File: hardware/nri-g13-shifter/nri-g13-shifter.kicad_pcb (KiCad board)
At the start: 2 copper layers, 96 x 92 mm, 39 parts, among them J1 NRI G-13 (10 pin), J2 RP2350-Plus, J3 +12V IN, Q1 BSS138, Q2 BSS138, Q3 BSS138, Q4 BSS138, Q5 BSS138, Q6 BSS138, Q7 BSS138

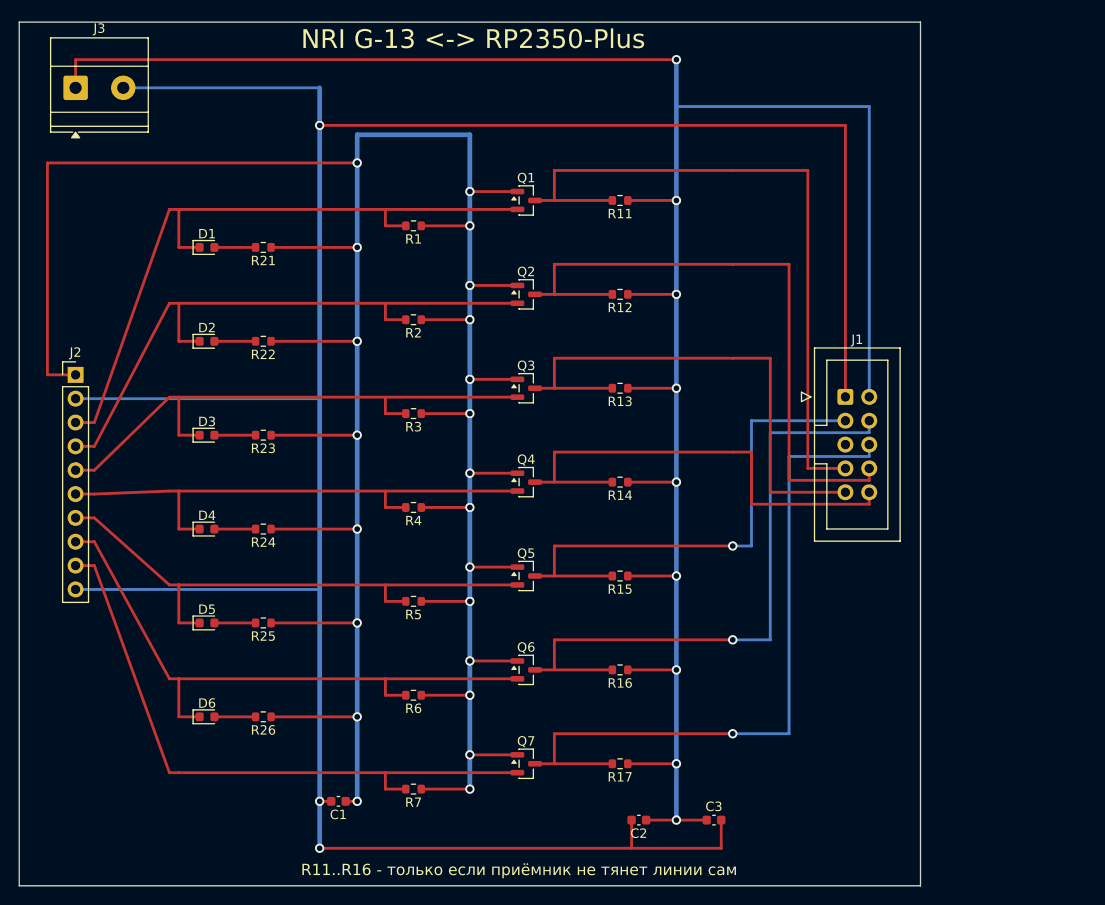
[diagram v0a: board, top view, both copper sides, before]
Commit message: Плата компактнее на треть, 12 В переехало в гребёнку
Клеммник убран, питание приёмника идёт через ту же гребёнку, что и
сигналы: отдельный разъём означал бы второй кабель к устройству, которое
и так стоит в тесном корпусе. Гребёнка стала двенадцатиконтактной, а
сигнальные выводы по-прежнему идут подряд и в порядке строк платы —
от этого веер разводки остаётся непересекающимся сам собой.

Плата 78x79 мм вместо 96x92, площадь меньше на 30%. Строка канала сжата
с 10 до 8 мм: полосы внутри неё не перекрываются по горизонтали, поэтому
индикатор и отвод к разъёму удалось посадить на одну высоту. По ширине
убраны просветы между шинами питания.

Попутно вылезла закономерность, которую пришлось записать в код: из двух
цепей, уходящих наверх по соседним вертикалям, выше должна идти та, что
взяла внешнюю вертикаль. Иначе её горизонталь пересекает чужую. DRC
поймал это дважды, пока порядок не встал правильно.

Проверено: ERC 0, DRC 0, неразведённых 0, расхождений со схемой 0.

Co-Authored-By: Claude Opus 5 (1M context) <noreply@anthropic.com>
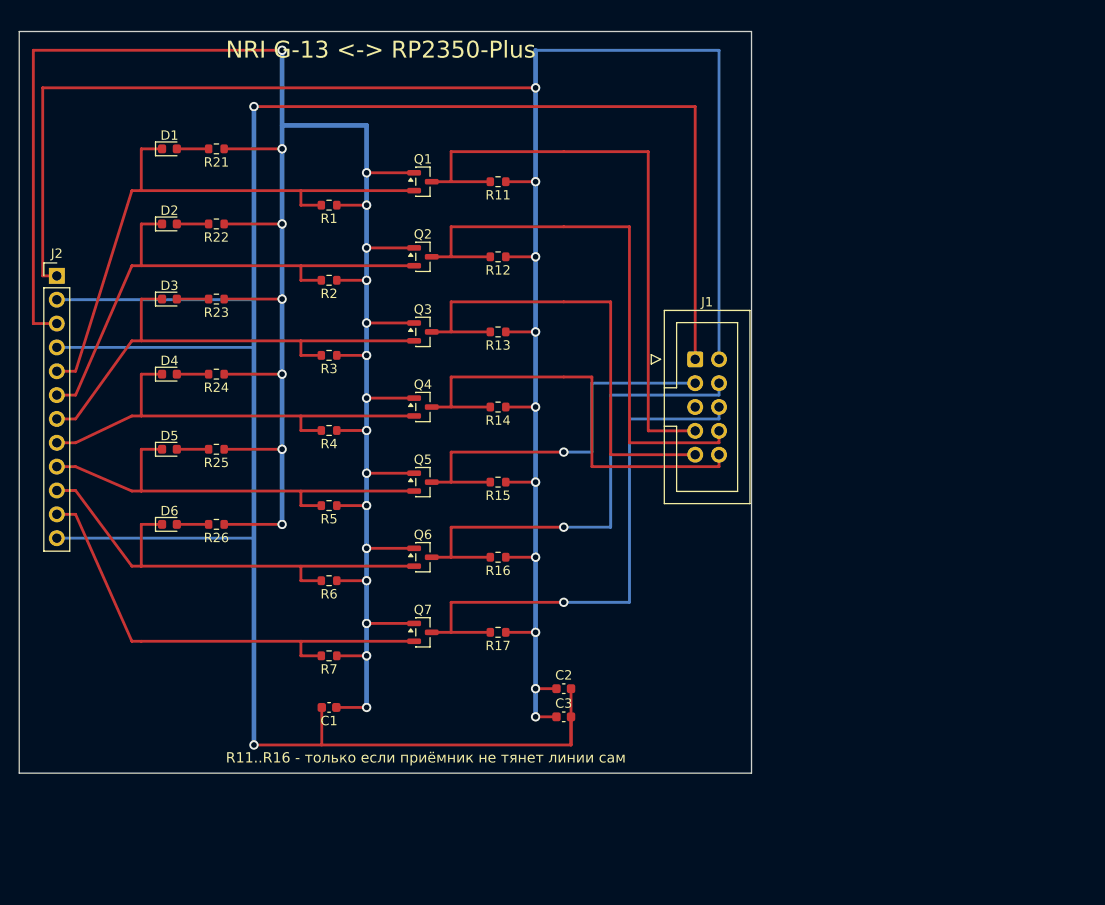
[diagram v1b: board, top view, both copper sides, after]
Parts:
- removed J3: +12V IN, TerminalBlock_Phoenix:TerminalBlock_Phoenix_MKDS-1,5-2-5.08_1x02_P5.08mm_Horizontal
- removed the R11 at (64.0, 24.0)
- removed the R12 at (64.0, 34.0)
- removed the R13 at (64.0, 44.0)
- removed the R14 at (64.0, 54.0)
- removed the R15 at (64.0, 64.0)
- removed the R16 at (64.0, 74.0)
- removed the R17 at (64.0, 84.0)
- removed the R21 at (26.0, 29.0)
- removed the R22 at (26.0, 39.0)
- removed the R23 at (26.0, 49.0)
- removed the R24 at (26.0, 59.0)
- removed the R25 at (26.0, 69.0)
- removed the R26 at (26.0, 79.0)
- added D1: LED, LED_SMD:LED_0603_1608Metric, F.Cu at (16.0, 18.5)
- added D2: LED, LED_SMD:LED_0603_1608Metric, F.Cu at (16.0, 26.5)
- added D3: LED, LED_SMD:LED_0603_1608Metric, F.Cu at (16.0, 34.5)
- added D4: LED, LED_SMD:LED_0603_1608Metric, F.Cu at (16.0, 42.5)
- added D5: LED, LED_SMD:LED_0603_1608Metric, F.Cu at (16.0, 50.5)
- added D6: LED, LED_SMD:LED_0603_1608Metric, F.Cu at (16.0, 58.5)
- added Q1: BSS138, Package_TO_SOT_SMD:SOT-23, F.Cu at (43.0, 22.0)
- added Q2: BSS138, Package_TO_SOT_SMD:SOT-23, F.Cu at (43.0, 30.0)
- added Q3: BSS138, Package_TO_SOT_SMD:SOT-23, F.Cu at (43.0, 38.0)
- added Q4: BSS138, Package_TO_SOT_SMD:SOT-23, F.Cu at (43.0, 46.0)
- added Q5: BSS138, Package_TO_SOT_SMD:SOT-23, F.Cu at (43.0, 54.0)
- added Q6: BSS138, Package_TO_SOT_SMD:SOT-23, F.Cu at (43.0, 62.0)
- added Q7: BSS138, Package_TO_SOT_SMD:SOT-23, F.Cu at (43.0, 70.0)
- J2: value RP2350-Plus -> RP2350-Plus + 12V; footprint Connector_PinHeader_2.54mm:PinHeader_1x10_P2.54mm_Vertical -> Connector_PinHeader_2.54mm:PinHeader_1x12_P2.54mm_Vertical
- R1: renamed from Q1; value BSS138 -> 10k; footprint Package_TO_SOT_SMD:SOT-23 -> Resistor_SMD:R_0603_1608Metric
- R2: renamed from Q2; value BSS138 -> 10k; footprint Package_TO_SOT_SMD:SOT-23 -> Resistor_SMD:R_0603_1608Metric
- R21: renamed from D1; value LED -> 1k; footprint LED_SMD:LED_0603_1608Metric -> Resistor_SMD:R_0603_1608Metric
- R22: renamed from D2; value LED -> 1k; footprint LED_SMD:LED_0603_1608Metric -> Resistor_SMD:R_0603_1608Metric
- R23: renamed from D3; value LED -> 1k; footprint LED_SMD:LED_0603_1608Metric -> Resistor_SMD:R_0603_1608Metric
- R24: renamed from D4; value LED -> 1k; footprint LED_SMD:LED_0603_1608Metric -> Resistor_SMD:R_0603_1608Metric
- R25: renamed from D5; value LED -> 1k; footprint LED_SMD:LED_0603_1608Metric -> Resistor_SMD:R_0603_1608Metric
- R26: renamed from D6; value LED -> 1k; footprint LED_SMD:LED_0603_1608Metric -> Resistor_SMD:R_0603_1608Metric
- R3: renamed from Q3; value BSS138 -> 10k; footprint Package_TO_SOT_SMD:SOT-23 -> Resistor_SMD:R_0603_1608Metric
- R4: renamed from Q4; value BSS138 -> 10k; footprint Package_TO_SOT_SMD:SOT-23 -> Resistor_SMD:R_0603_1608Metric
- R5: renamed from Q5; value BSS138 -> 10k; footprint Package_TO_SOT_SMD:SOT-23 -> Resistor_SMD:R_0603_1608Metric
- R6: renamed from Q6; value BSS138 -> 10k; footprint Package_TO_SOT_SMD:SOT-23 -> Resistor_SMD:R_0603_1608Metric
- R7: renamed from Q7; value BSS138 -> 10k; footprint Package_TO_SOT_SMD:SOT-23 -> Resistor_SMD:R_0603_1608Metric
- moved R7 23.9 mm to (33.0, 72.5), turned to 180 degrees
- moved R6 23.0 mm to (33.0, 64.5), turned to 180 degrees
- moved R5 22.3 mm to (33.0, 56.5), turned to 180 degrees
- moved R4 21.7 mm to (33.0, 48.5), turned to 180 degrees
- moved R3 21.3 mm to (33.0, 40.5), turned to 180 degrees
- moved R2 21.1 mm to (33.0, 32.5), turned to 180 degrees
- moved R1 21.0 mm to (33.0, 24.5), turned to 180 degrees
- moved R26 20.5 mm to (21.0, 58.5), turned to 180 degrees
- moved C3 19.4 mm to (58.0, 79.0)
- moved R17 19.0 mm to (51.0, 70.0)
- moved R25 18.5 mm to (21.0, 50.5), turned to 180 degrees
- moved R16 17.2 mm to (51.0, 62.0)
- moved R24 16.5 mm to (21.0, 42.5), turned to 180 degrees
- moved J1 16.5 mm to (72.0, 40.9)
- moved C2 16.1 mm to (58.0, 76.0), turned to 0 degrees
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- renumbered R1 to R11, R2 to R12, R3 to R13, R4 to R14, R5 to R15, R6 to R16, R7 to R17
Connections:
- J2 pad 1: +3V3 -> +12V
- J2 pad 10: GND -> /GP8
- J2 pad 3: /GP3 -> +3V3
- J2 pad 4: /GP4 -> GND
- J2 pad 5: /GP5 -> /GP3
- J2 pad 6: /GP6 -> /GP4
- J2 pad 7: /GP7 -> /GP5
- J2 pad 8: /GP8 -> /GP6
- J2 pad 9: /GP9 -> /GP7
- R11 pad 1: +3V3 -> +12V
- R11 pad 2: /GP3 -> /LINE1
- R12 pad 1: +3V3 -> +12V
- R12 pad 2: /GP4 -> /LINE2
- R13 pad 1: +3V3 -> +12V
- R13 pad 2: /GP5 -> /LINE3
- R14 pad 1: +3V3 -> +12V
- R14 pad 2: /GP6 -> /LINE4
- R15 pad 1: +3V3 -> +12V
- R15 pad 2: /GP7 -> /LINE5
- R16 pad 1: +3V3 -> +12V
- R16 pad 2: /GP8 -> /LINE6
- R17 pad 1: +3V3 -> +12V
- R17 pad 2: /GP9 -> /INHIBIT
- R21 pad 1: /GP3 -> +3V3
- R22 pad 1: /GP4 -> +3V3
- R23 pad 1: /GP5 -> +3V3
- R24 pad 1: /GP6 -> +3V3
- R25 pad 1: /GP7 -> +3V3
- R26 pad 1: /GP8 -> +3V3
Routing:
- net +3V3: track 339.2 -> 277.5 mm
- net GND: track 288.8 -> 251.7 mm, vias 3 -> 2
- net +12V: track 242.1 -> 224.2 mm, vias 9 -> 10
- net /INHIBIT: track 75.8 -> 58.8 mm
- net /GP9: track 66.5 -> 50.6 mm
- net /LINE6: track 68.3 -> 53.3 mm
- net /GP8: track 65.9 -> 52.5 mm
- net /LINE5: track 55.8 -> 42.8 mm
- net /GP7: track 60.0 -> 49.0 mm
- net /GP3: track 73.3 -> 62.6 mm
- net /LINE1: track 74.2 -> 65.2 mm
- net /GP4: track 66.5 -> 57.5 mm
- net /GP6: track 57.3 -> 49.1 mm
- net /GP5: track 60.4 -> 52.7 mm
- net /LINE2: track 69.3 -> 62.3 mm
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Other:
- board size 96 x 92 mm -> 78 x 79 mm

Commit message: Заливка землёй по обоим слоям, шины питания шире
Обе заливки получились сплошными: сигналы идут наверху горизонтальными
полосами, питание внизу вертикальными, и ни то, ни другое не режет плату
поперёк.

Дорожки земли под заливкой оставлены намеренно. Заливка на плотной плате
может разорваться на куски, и надеяться, что все они окажутся связаны,
нельзя, — а дорожка связывает гарантированно.

Сшивающие отверстия стоят строго на этих дорожках. Первый заход поставил
их по нижнему краю в чистом поле, и DRC показал тринадцать висящих: пока
заливка вокруг не легла, отверстие связью не считается — ни для проверки,
ни на плате, если медь вокруг окажется отрезанной.

island_removal_mode 0: куски заливки без связи выбрасываются. С режимом 1
они остаются, и KiCad честно называет их изолированной медью — то есть
антенной.

Шины 3.3 В и 12 В расширены до 1.2 мм, отводы питания до 0.8. Ток тут
копеечный, дело в надёжности: такую дорожку труднее подорвать при монтаже.
Ширина выбирается по цепи внутри seg(), а не задаётся на каждом вызове, —
иначе её легко забыть на одном отводе из семнадцати.

Заливку заполняет KiCad, а не скрипт, поэтому в порядок сборки добавлен
--refill-zones --save-board. Без него плата откроется с пустыми зонами.

Проверено: DRC 0, неразведённых 0, расхождений со схемой 0.

Co-Authored-By: Claude Opus 5 (1M context) <noreply@anthropic.com>
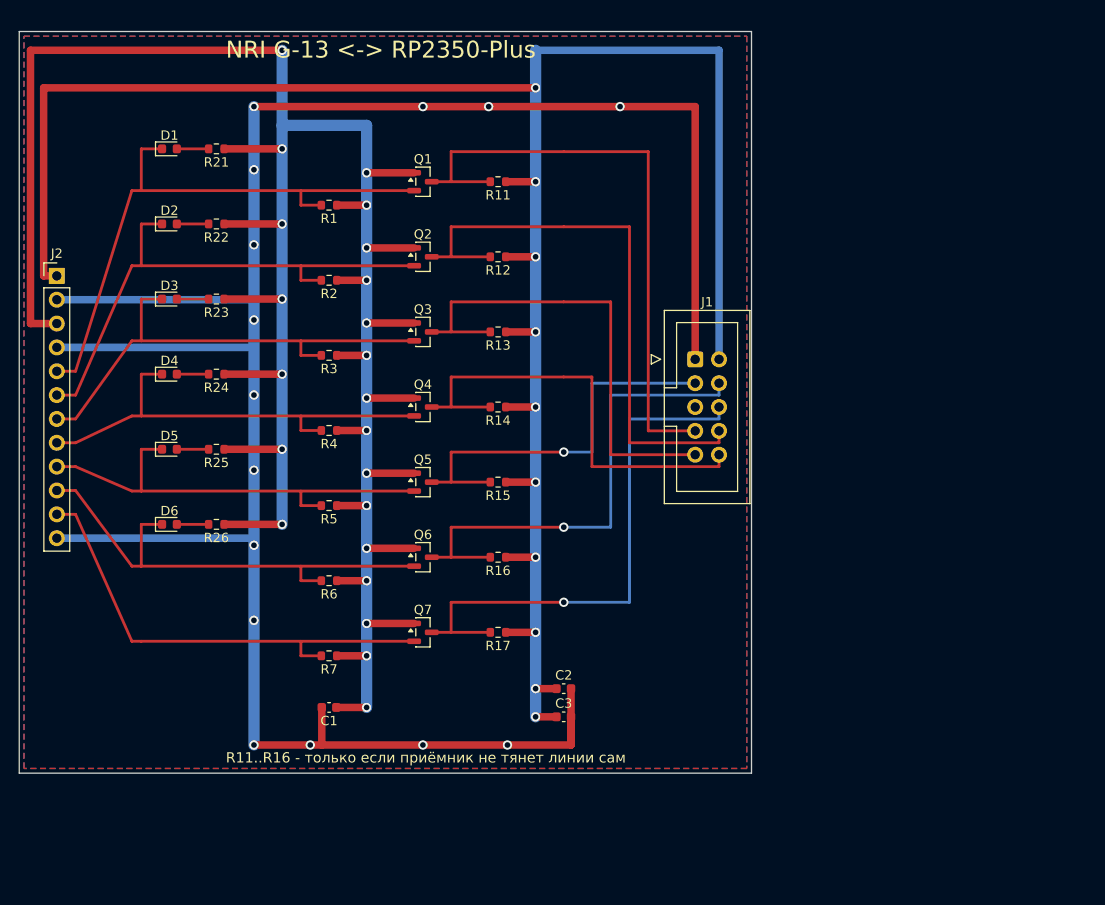
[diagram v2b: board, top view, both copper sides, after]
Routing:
- net +3V3: track 277.5 -> 278.1 mm
- net GND: vias 2 -> 15
- added copper zone on B.Cu, net GND
- added copper zone on F.Cu, net GND

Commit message: Артикулы JLCPCB и исправление номинала C3
Артикулы проставлены в схеме, при компонентах, и оттуда попадают и в
bom.csv, и в плату. Все сверены по каталогу, а не восстановлены по
памяти: неверный код — это не опечатка, а другая деталь на плате.

Подбор артикулов и вскрыл ошибку: C3 стоял на 10 мкФ, а в корпусе 0603
такая ёмкость бывает только на 10 вольт. Сидит эта банка на шине 12 В,
то есть номинал был просто неработоспособен. В схеме этого не видно —
там написано «10u» без напряжения, — а в каталоге написано. Поставлено
1 мкФ 50 В, тока тут копеечный и ёмкости хватает с запасом.

BSS138 оставлен расширенной позицией. Базовый 2N7002 сэкономил бы плату
за настройку станка, но у него порог отпирания вдвое выше, а весь смысл
каскада в том, чтобы он открывался от 3.3 В.

Артикул переносится и в посадочные места платы: иначе сверка со схемой
считает поле потерянным, а на монтаж уедет плата без указания, что
ставить.

Проверено: ERC 0, DRC 0, расхождений со схемой 0.

Co-Authored-By: Claude Opus 5 (1M context) <noreply@anthropic.com>
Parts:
- removed the Q1 at (43.0, 22.0)
- removed the Q5 at (43.0, 54.0)
- removed the R13 at (51.0, 38.0)
- removed the R21 at (21.0, 18.5)
- removed the R24 at (21.0, 42.5)
- removed the R5 at (33.0, 56.5)
- added D5: LED, LED_SMD:LED_0603_1608Metric, F.Cu at (16.0, 50.5)
- added Q2: BSS138, Package_TO_SOT_SMD:SOT-23, F.Cu at (43.0, 30.0)
- added Q6: BSS138, Package_TO_SOT_SMD:SOT-23, F.Cu at (43.0, 62.0)
- added R11: 10k, Resistor_SMD:R_0603_1608Metric, F.Cu at (51.0, 22.0)
- added R16: 10k, Resistor_SMD:R_0603_1608Metric, F.Cu at (51.0, 62.0)
- added R23: 1k, Resistor_SMD:R_0603_1608Metric, F.Cu at (21.0, 34.5)
- C3: value 10u -> 1u
- Q1: renamed from R11; value 10k -> BSS138; footprint Resistor_SMD:R_0603_1608Metric -> Package_TO_SOT_SMD:SOT-23
- R13: renamed from R23; value 1k -> 10k
- R21: renamed from Q2; value BSS138 -> 1k; footprint Package_TO_SOT_SMD:SOT-23 -> Resistor_SMD:R_0603_1608Metric
- R24: renamed from D5; value LED -> 1k; footprint LED_SMD:LED_0603_1608Metric -> Resistor_SMD:R_0603_1608Metric
- moved R13 30.2 mm to (51.0, 38.0)
- moved R21 24.8 mm to (21.0, 18.5), turned to 180 degrees
- moved R5 18.8 mm to (33.0, 56.5)
- moved R24 9.43 mm to (21.0, 42.5), turned to 180 degrees
- moved Q1 8.00 mm to (43.0, 22.0), turned to 0 degrees
- moved Q5 8.00 mm to (43.0, 54.0)
- renumbered Q6 to Q5, R16 to R5
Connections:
- Q1 pad 1: +12V -> +3V3
- Q1 pad 2: /LINE1 -> /GP3
- Q5 pad 2: /GP8 -> /GP7
- Q5 pad 3: /LINE6 -> /LINE5
- R13 pad 1: +3V3 -> +12V
- R13 pad 2: Net-(D3-A) -> /LINE3
- R21 pad 2: /GP4 -> Net-(D1-A)
- R24 pad 1: /GP7 -> +3V3
- R24 pad 2: Net-(D5-A) -> Net-(D4-A)
- R5 pad 1: +12V -> +3V3
- R5 pad 2: /LINE6 -> /GP7

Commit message: Светодиод красный, резистор 470 Ом: зелёный не зажёгся бы вовсе
JLCPCB не сопоставил C72043 — снят с наличия. При проверке замены
выяснилось худшее: у зелёного в корпусе 0603 прямое напряжение 3.3 В,
ровно столько же, сколько на шине, от которой он питается. Через 1 кОм
ток получался бы нулевой, и шесть индикаторов просто не горели бы.

Красный C2286 (KT-0603R): 1.8…2.4 В, склад под четыре миллиона штук.
Резистор заодно уменьшен до 470 Ом — около 3 мА, для вспышки длиной
100 мс этого хватает уверенно.

Второй раз подряд ошибку вскрывает подбор артикулов, а не схема: в
номиналах «10u» и «LED» нет ни рабочего напряжения, ни прямого падения,
а в каталоге есть.

Проверено: ERC 0, DRC 0, расхождений со схемой 0.

Co-Authored-By: Claude Opus 5 (1M context) <noreply@anthropic.com>
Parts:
- R21, R22, R23, R24, R25, R26: value 1k -> 470
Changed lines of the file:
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@@
 			)
 		)
-		(property "Value" "1k"
+		(property "Value" "470"
 			(at 0 1.43 180)
 			(layer "F.Fab")
@@
 			)
 		)
-		(property "LCSC" "C21190"
+		(property "LCSC" "C23179"
 			(at 0 0 0)
 			(unlocked yes)
@@
 			)
 		)
-		(property "Value" "1k"
+		(property "Value" "470"
 			(at 0 1.43 180)
 			(layer "F.Fab")
@@
 			)
 		)
-		(property "LCSC" "C21190"
+		(property "LCSC" "C23179"
 			(at 0 0 0)
 			(unlocked yes)
@@
 			)
 		)
-		(property "Value" "1k"
+		(property "Value" "470"
 			(at 0 1.43 180)
 			(layer "F.Fab")
@@
 			)
 		)
-		(property "LCSC" "C21190"
+		(property "LCSC" "C23179"
 			(at 0 0 0)
 			(unlocked yes)
@@
 			)
 		)
-		(property "Value" "1k"
+		(property "Value" "470"
 			(at 0 1.43 180)
 			(layer "F.Fab")
@@
 			)
 		)
-		(property "LCSC" "C21190"
+		(property "LCSC" "C23179"
 			(at 0 0 0)
 			(unlocked yes)
@@
 			)
 		)
-		(property "LCSC" "C72043"
+		(property "LCSC" "C2286"
 			(at 0 0 0)
 			(unlocked yes)
@@
 			)
 		)
-		(property "Value" "1k"
+		(property "Value" "470"
 			(at 0 1.43 180)
 			(layer "F.Fab")
@@
 			)
 		)
-		(property "LCSC" "C21190"
+		(property "LCSC" "C23179"
 			(at 0 0 0)
 			(unlocked yes)
@@
 			)
 		)
-		(property "LCSC" "C72043"
+		(property "LCSC" "C2286"
 			(at 0 0 0)
 			(unlocked yes)
@@
 			)
 		)
-		(property "LCSC" "C72043"
+		(property "LCSC" "C2286"
 			(at 0 0 0)
 			(unlocked yes)
@@
 			)
 		)
-		(property "LCSC" "C72043"
+		(property "LCSC" "C2286"
 			(at 0 0 0)
 			(unlocked yes)
@@
 			)
 		)
-		(property "LCSC" "C72043"
+		(property "LCSC" "C2286"
 			(at 0 0 0)
 			(unlocked yes)
@@
 			)
 		)
-		(property "LCSC" "C72043"
+		(property "LCSC" "C2286"
 			(at 0 0 0)
 			(unlocked yes)
@@
 			)
 		)
-		(property "Value" "1k"
+		(property "Value" "470"
 			(at 0 1.43 180)
 			(layer "F.Fab")
@@
 			)
 		)
-		(property "LCSC" "C21190"
+		(property "LCSC" "C23179"
 			(at 0 0 0)
 			(unlocked yes)
